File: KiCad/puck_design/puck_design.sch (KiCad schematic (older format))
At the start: 24 parts

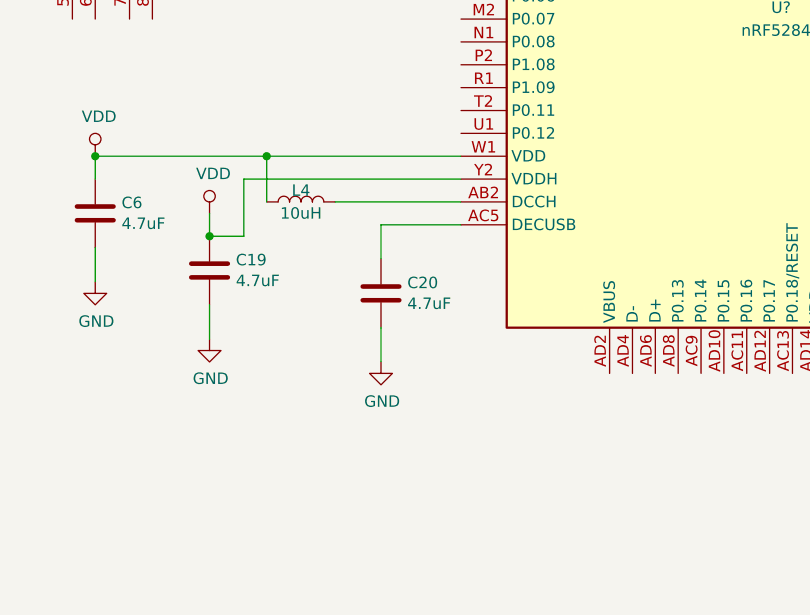
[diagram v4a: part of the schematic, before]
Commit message: Removed USB features, added battery (VDDH) to schem
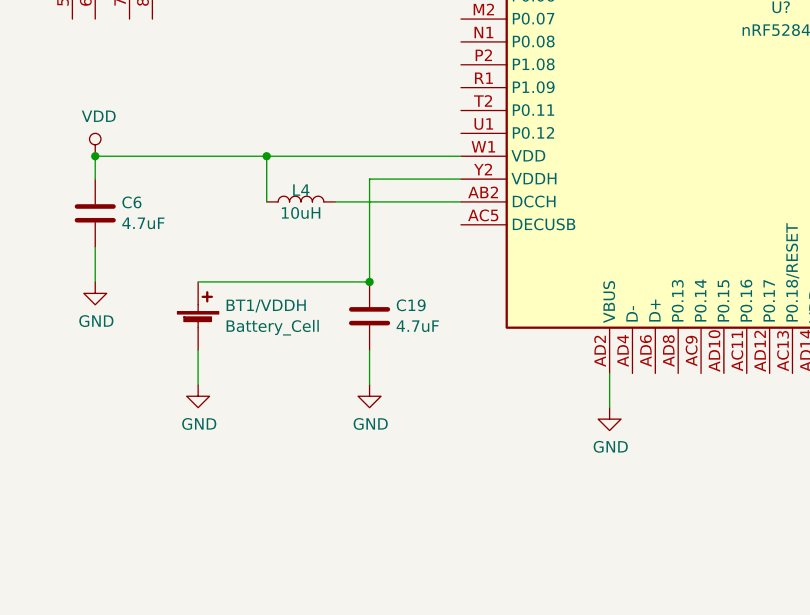
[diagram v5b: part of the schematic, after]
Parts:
- removed C20: 4.7uF, symbol Device:C
- added BT1/VDDH: Battery_Cell, symbol Device:Battery_Cell
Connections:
- net GND: now also U?.AD2 (VBUS), BT1/VDDH.2 (-)
- net VDD: no longer C19.1, U?.Y2 (VDDH)
- new net: BT1/VDDH.1 (+), C19.1, U?.Y2 (VDDH)
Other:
- moved on the sheet: C19
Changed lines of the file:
@@
-$EndComp
-$Comp
-L Device:C C20
-U 1 1 5BF5920B
-P 3500 5650
-F 0 "C20" H 3615 5696 50  0000 L CNN
-F 1 "4.7uF" H 3615 5605 50  0000 L CNN
-F 2 "" H 3538 5500 50  0001 C CNN
-F 3 "~" H 3500 5650 50  0001 C CNN
-	1    3500 5650
-	1    0    0    -1
 $EndComp
 $Comp
 L Device:C C19
 U 1 1 5BF59255
-P 2750 5550
-F 0 "C19" H 2865 5596 50  0000 L CNN
-F 1 "4.7uF" H 2865 5505 50  0000 L CNN
-F 2 "" H 2788 5400 50  0001 C CNN
-F 3 "~" H 2750 5550 50  0001 C CNN
-	1    2750 5550
+P 3450 5750
+F 0 "C19" H 3565 5796 50  0000 L CNN
+F 1 "4.7uF" H 3565 5705 50  0000 L CNN
+F 2 "" H 3488 5600 50  0001 C CNN
+F 3 "~" H 3450 5750 50  0001 C CNN
+	1    3450 5750
 	1    0    0    -1
 $EndComp
@@
 $Comp
 L power:GND #PWR?
-U 1 1 5BF5ED93
-P 3500 5950
-F 0 "#PWR?" H 3500 5700 50  0001 C CNN
-F 1 "GND" H 3505 5777 50  0000 C CNN
-F 2 "" H 3500 5950 50  0001 C CNN
-F 3 "" H 3500 5950 50  0001 C CNN
-	1    3500 5950
-	1    0    0    -1
-$EndComp
-$Comp
-L power:GND #PWR?
 U 1 1 5BF5EDB2
-P 2750 5850
-F 0 "#PWR?" H 2750 5600 50  0001 C CNN
-F 1 "GND" H 2755 5677 50  0000 C CNN
-F 2 "" H 2750 5850 50  0001 C CNN
-F 3 "" H 2750 5850 50  0001 C CNN
-	1    2750 5850
+P 3450 6050
+F 0 "#PWR?" H 3450 5800 50  0001 C CNN
+F 1 "GND" H 3455 5877 50  0000 C CNN
+F 2 "" H 3450 6050 50  0001 C CNN
+F 3 "" H 3450 6050 50  0001 C CNN
+	1    3450 6050
 	1    0    0    -1
 $EndComp
@@
 	5550 6700 5550 6750
 Wire Wire Line
-	3850 5350 3500 5350
-Wire Wire Line
-	3500 5350 3500 5500
-Wire Wire Line
-	3500 5800 3500 5950
-Wire Wire Line
 	3850 5250 3300 5250
 Wire Wire Line
@@
 	3000 5050 2250 5050
 Wire Wire Line
-	2750 5700 2750 5850
-$Comp
-L power:VDD #PWR?
-U 1 1 5BF7EEA5
-P 2750 5300
-F 0 "#PWR?" H 2750 5150 50  0001 C CNN
-F 1 "VDD" H 2767 5473 50  0000 C CNN
-F 2 "" H 2750 5300 50  0001 C CNN
-F 3 "" H 2750 5300 50  0001 C CNN
-	1    2750 5300
-	1    0    0    -1
-$EndComp
-Wire Wire Line
-	3850 5150 2900 5150
-Wire Wire Line
-	2900 5150 2900 5400
-Wire Wire Line
-	2900 5400 2750 5400
-Wire Wire Line
-	2750 5300 2750 5400
-Connection ~ 2750 5400
+	3450 5900 3450 6050
 Wire Wire Line
 	4800 1500 4900 1500
@@
 Wire Wire Line
 	5300 2900 5300 3000
+$Comp
+L power:GND #PWR?
+U 1 1 5BF642BA
+P 4500 6150
+F 0 "#PWR?" H 4500 5900 50  0001 C CNN
+F 1 "GND" H 4505 5977 50  0000 C CNN
+F 2 "" H 4500 6150 50  0001 C CNN
+F 3 "" H 4500 6150 50  0001 C CNN
+	1    4500 6150
+	1    0    0    -1
+$EndComp
+Wire Wire Line
+	4500 6000 4500 6150
+$Comp
+L Device:Battery_Cell BT1/VDDH
+U 1 1 5BF7601E
+P 2700 5800
+F 0 "BT1/VDDH" H 2818 5896 50  0000 L CNN
+F 1 "Battery_Cell" H 2818 5805 50  0000 L CNN
+F 2 "" V 2700 5860 50  0001 C CNN
+F 3 "~" V 2700 5860 50  0001 C CNN
+	1    2700 5800
+	1    0    0    -1
+$EndComp
+Wire Wire Line
+	2700 5600 3450 5600
+Wire Wire Line
+	3850 5150 3450 5150
+Wire Wire Line
+	3450 5150 3450 5600
+Connection ~ 3450 5600
+$Comp
+L power:GND #PWR?
+U 1 1 5BF8D1C5
+P 2700 6050
+F 0 "#PWR?" H 2700 5800 50  0001 C CNN
+F 1 "GND" H 2705 5877 50  0000 C CNN
+F 2 "" H 2700 6050 50  0001 C CNN
+F 3 "" H 2700 6050 50  0001 C CNN
+	1    2700 6050
+	1    0    0    -1
+$EndComp
+Wire Wire Line
+	2700 5900 2700 6050
 $EndSCHEMATC

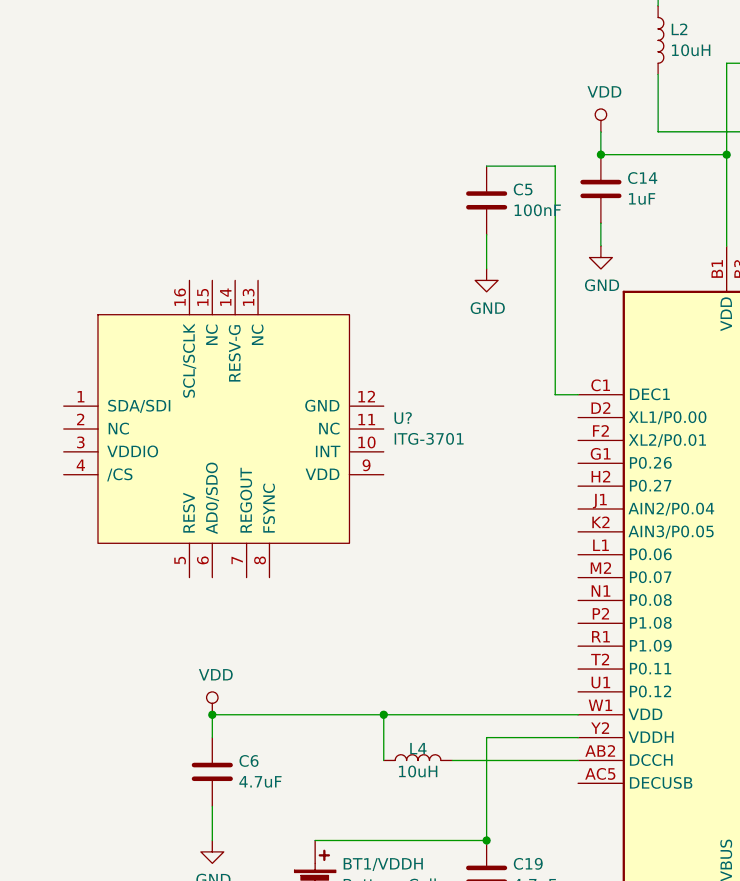
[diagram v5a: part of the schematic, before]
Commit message: Initial gyro connections
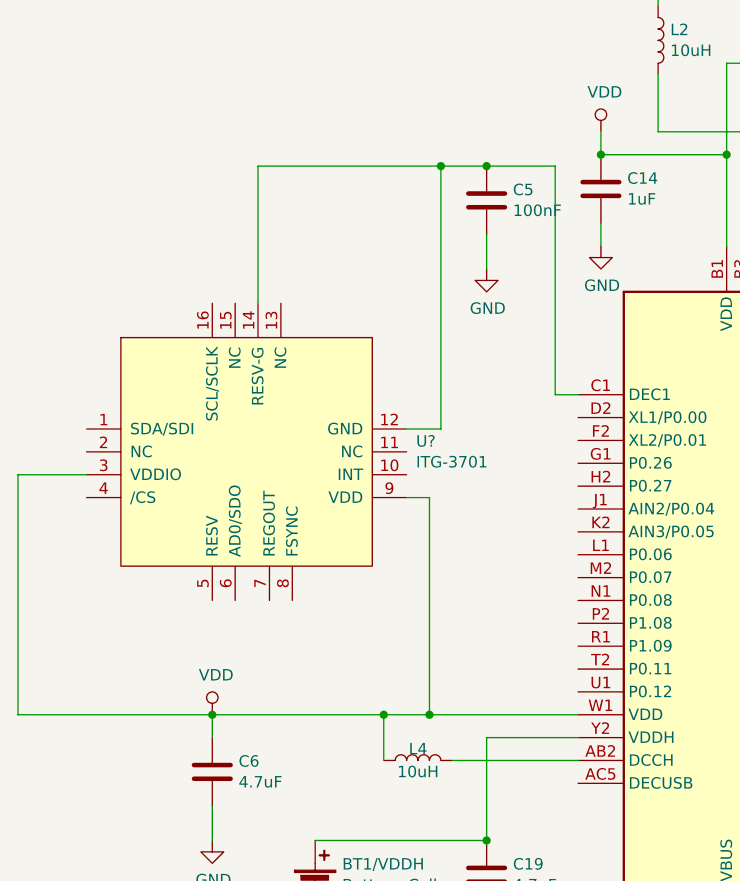
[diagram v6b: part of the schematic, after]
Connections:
- net VDD: now also U?.3 (VDDIO), U?.9 (VDD)
- net at U?.12 (GND): now also C5.1, U?.14 (RESV-G), U?.C1 (DEC1)
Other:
- moved on the sheet: U?
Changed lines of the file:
@@
 L puck_library:ITG-3701 U?
 U 1 1 5BF49DCF
-P 2300 3850
-F 0 "U?" H 3041 3946 50  0000 L CNN
-F 1 "ITG-3701" H 3041 3855 50  0000 L CNN
-F 2 "" H 2300 3850 50  0001 C CNN
-F 3 "" H 2300 3850 50  0001 C CNN
-	1    2300 3850
+P 2400 3950
+F 0 "U?" H 3141 4046 50  0000 L CNN
+F 1 "ITG-3701" H 3141 3955 50  0000 L CNN
+F 2 "" H 2400 3950 50  0001 C CNN
+F 3 "" H 2400 3950 50  0001 C CNN
+	1    2400 3950
 	1    0    0    -1
 $EndComp
@@
 	3850 5250 3300 5250
 Wire Wire Line
-	3850 5050 3000 5050
+	3850 5050 3200 5050
 Wire Wire Line
 	2250 5150 2250 5050
@@
 Wire Wire Line
 	2700 5900 2700 6050
+Wire Wire Line
+	3200 5050 3200 4100
+Wire Wire Line
+	3200 4100 3100 4100
+Connection ~ 3200 5050
+Wire Wire Line
+	3200 5050 3000 5050
+Wire Wire Line
+	3100 3800 3250 3800
+Wire Wire Line
+	3250 3800 3250 2650
+Wire Wire Line
+	3250 2650 3450 2650
+Connection ~ 3450 2650
+Wire Wire Line
+	2450 3250 2450 2650
+Wire Wire Line
+	2450 2650 3250 2650
+Connection ~ 3250 2650
+Wire Wire Line
+	1700 4000 1400 4000
+Wire Wire Line
+	1400 4000 1400 5050
+Wire Wire Line
+	1400 5050 2250 5050
 $EndSCHEMATC

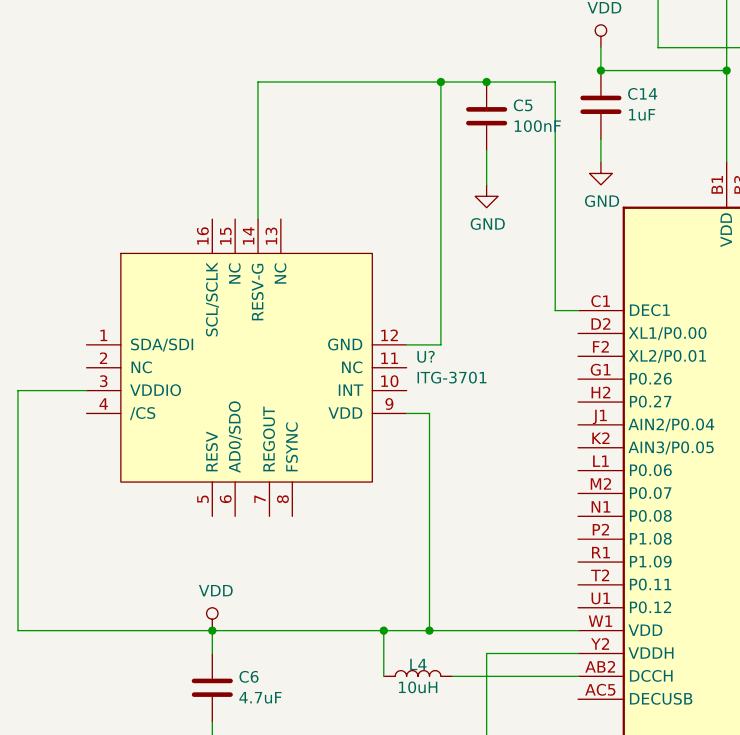
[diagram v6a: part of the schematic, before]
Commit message: Added remaining connections for gyro
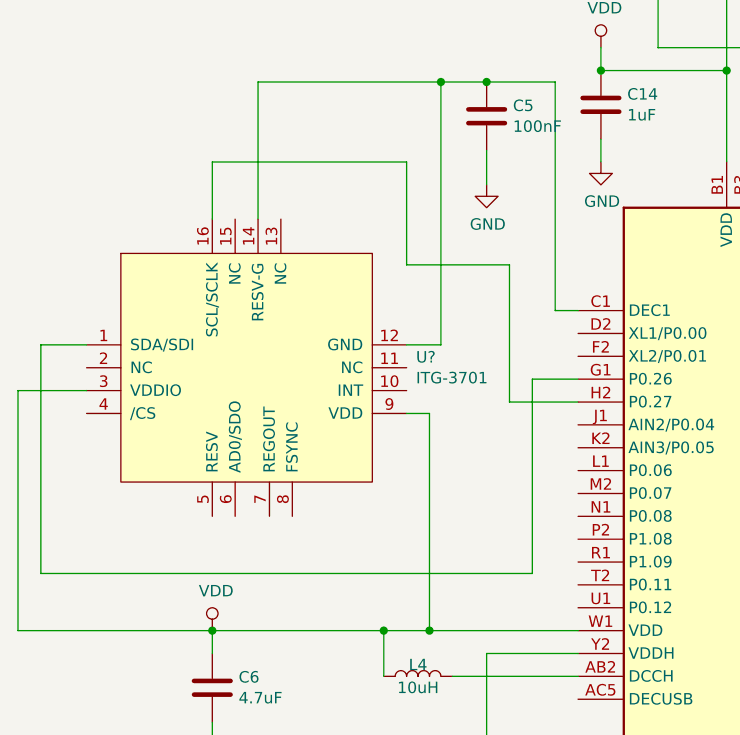
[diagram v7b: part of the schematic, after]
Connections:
- net at U?.1 (SDA/SDI): now also U?.G1 (P0.26)
- net at U?.16 (SCL/SCLK): now also U?.H2 (P0.27)
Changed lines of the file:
@@
 Wire Wire Line
 	1400 5050 2250 5050
+Wire Wire Line
+	3850 4050 3550 4050
+Wire Wire Line
+	3550 3450 3100 3450
+Wire Wire Line
+	3100 3450 3100 3000
+Wire Wire Line
+	3100 3000 2250 3000
+Wire Wire Line
+	2250 3000 2250 3250
+Wire Wire Line
+	3550 3450 3550 4050
+Wire Wire Line
+	3850 3950 3650 3950
+Wire Wire Line
+	3650 3950 3650 4800
+Wire Wire Line
+	3650 4800 1500 4800
+Wire Wire Line
+	1500 4800 1500 3800
+Wire Wire Line
+	1500 3800 1700 3800
 $EndSCHEMATC
